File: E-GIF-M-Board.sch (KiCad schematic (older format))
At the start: 0 parts

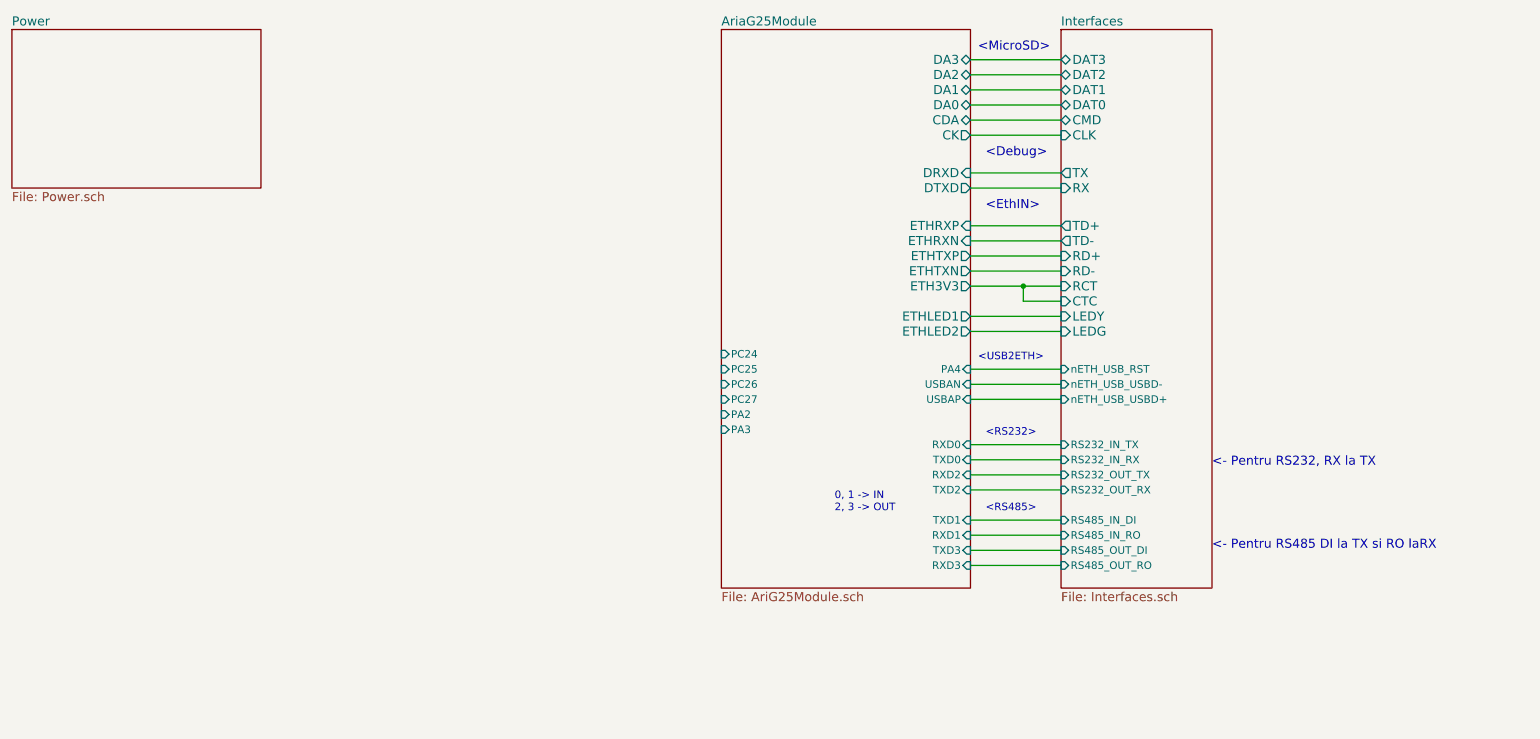
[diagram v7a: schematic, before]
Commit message: Added to scheamtic.
Added reset circuit for Aiya, power led for 3V3 line, USB type A connectors for USBB and USBC.
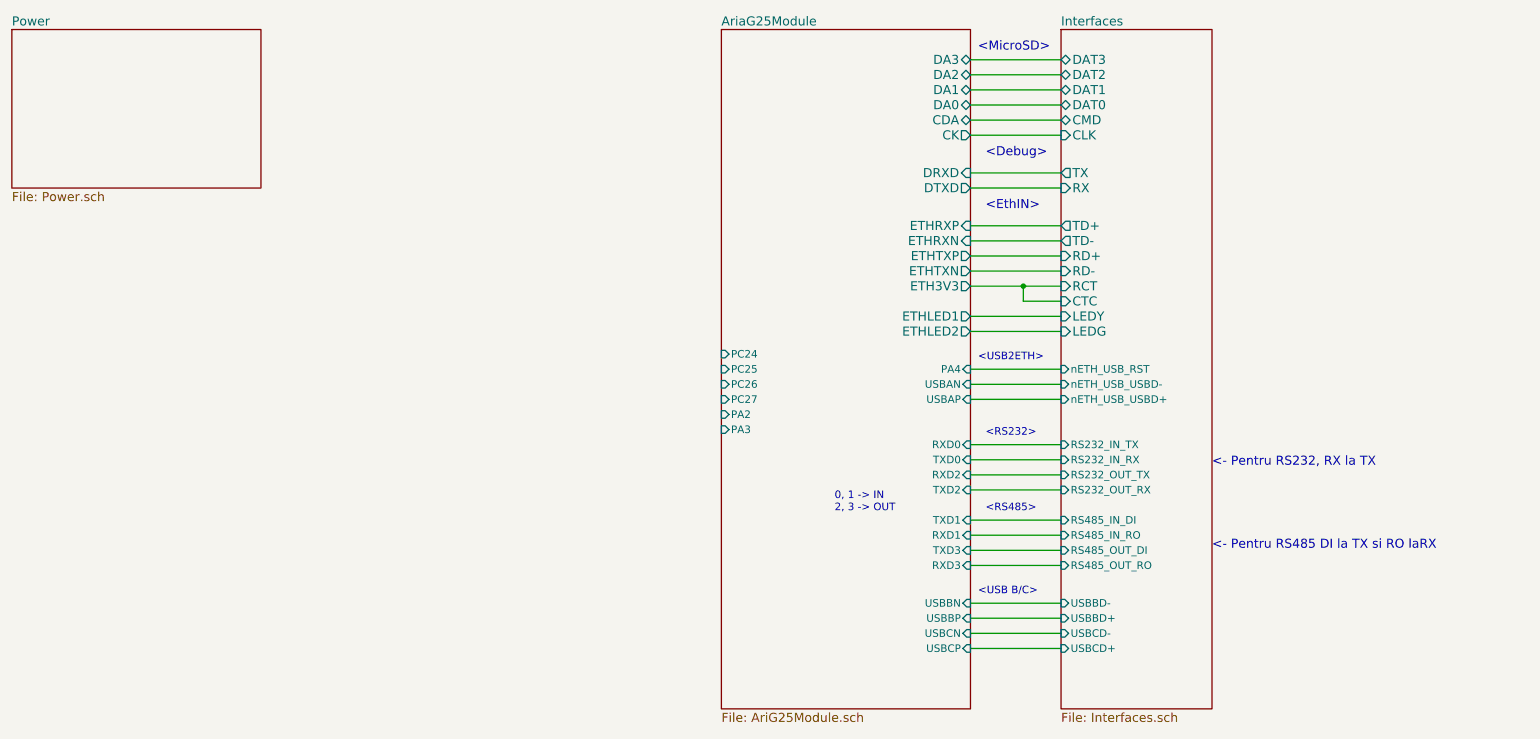
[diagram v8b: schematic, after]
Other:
- note added: "<USB B/C>"
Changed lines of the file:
@@
 LIBS:w_connectors
 LIBS:max-lin
+LIBS:IHE
 LIBS:E-GIF-M-Board-cache
 EELAYER 25 0
@@
 $EndSheet
 $Sheet
-S 5650 1100 1650 3700
+S 5650 1100 1650 4500
 U 587D31F1
 F0 "AriaG25Module" 60
@@
 F32 "PA3" I L 5650 3750 50
 F33 "PA4" I R 7300 3350 50
+F34 "USBBN" I R 7300 4900 50
+F35 "USBBP" I R 7300 5000 50
+F36 "USBCP" I R 7300 5200 50
+F37 "USBCN" I R 7300 5100 50
 $EndSheet
 $Sheet
-S 7900 1100 1000 3700
+S 7900 1100 1000 4500
 U 587FE94B
 F0 "Interfaces" 60
@@
 F27 "RS485_OUT_DI" I L 7900 4550 50
 F28 "RS485_OUT_RO" I L 7900 4650 50
+F29 "USBBD-" I L 7900 4900 50
+F30 "USBBD+" I L 7900 5000 50
+F31 "USBCD-" I L 7900 5100 50
+F32 "USBCD+" I L 7900 5200 50
 $EndSheet
 Text Notes 7350 1250 0    60   ~ 0
 <MicroSD>
+Text Notes 7400 1950 0    60   ~ 0
+<Debug>
+Text Notes 7400 2300 0    60   ~ 0
+<EthIN>
+Text Notes 6400 4300 0    50   ~ 0
+0, 1 -> IN\n2, 3 -> OUT
+Text Notes 7350 3300 0    50   ~ 0
+<USB2ETH>
+Text Notes 7400 3800 0    50   ~ 0
+<RS232>
+Text Notes 7400 4300 0    50   ~ 0
+<RS485>
+Text Notes 8900 4000 0    60   ~ 0
+<- Pentru RS232, RX la TX
+Text Notes 8900 4550 0    60   ~ 0
+<- Pentru RS485 DI la TX si RO laRX
 Wire Wire Line
 	7300 1300 7900 1300
@@
 Wire Wire Line
 	7300 1800 7900 1800
-Text Notes 7400 1950 0    60   ~ 0
-<Debug>
-Text Notes 7400 2300 0    60   ~ 0
-<EthIN>
 Wire Wire Line
 	7300 2150 7900 2150
@@
 Wire Wire Line
 	7300 4650 7900 4650
-Text Notes 6400 4300 0    50   ~ 0
-0, 1 -> IN\n2, 3 -> OUT
 Wire Wire Line
 	7300 3850 7900 3850
@@
 Wire Wire Line
 	7300 3550 7900 3550
-Text Notes 7350 3300 0    50   ~ 0
-<USB2ETH>
-Text Notes 7400 3800 0    50   ~ 0
-<RS232>
-Text Notes 7400 4300 0    50   ~ 0
-<RS485>
-Text Notes 8900 4000 0    60   ~ 0
-<- Pentru RS232, RX la TX
-Text Notes 8900 4550 0    60   ~ 0
-<- Pentru RS485 DI la TX si RO laRX
+Wire Wire Line
+	7300 4900 7900 4900
+Wire Wire Line
+	7300 5000 7900 5000
+Wire Wire Line
+	7300 5100 7900 5100
+Wire Wire Line
+	7300 5200 7900 5200
+Text Notes 7350 4850 0    50   ~ 0
+<USB B/C>
 $EndSCHEMATC
